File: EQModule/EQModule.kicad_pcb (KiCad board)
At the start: 2 copper layers, 30 x 38 mm, 13 parts, among them J1 SigIn, J2 SigOut, J3 TreblePot, J4 BassPot, J5 MidPot, J6 VolPot

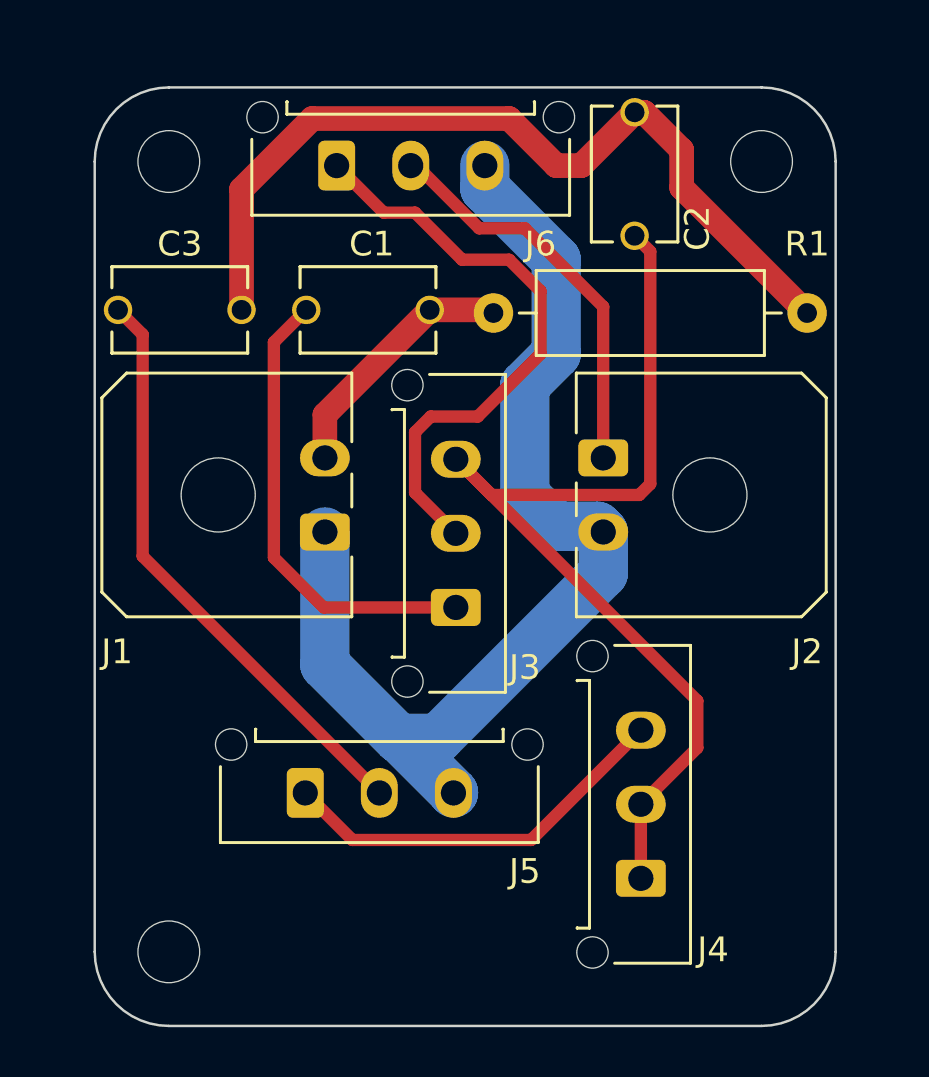
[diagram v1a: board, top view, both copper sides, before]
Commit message: Standardized hole size across all boards
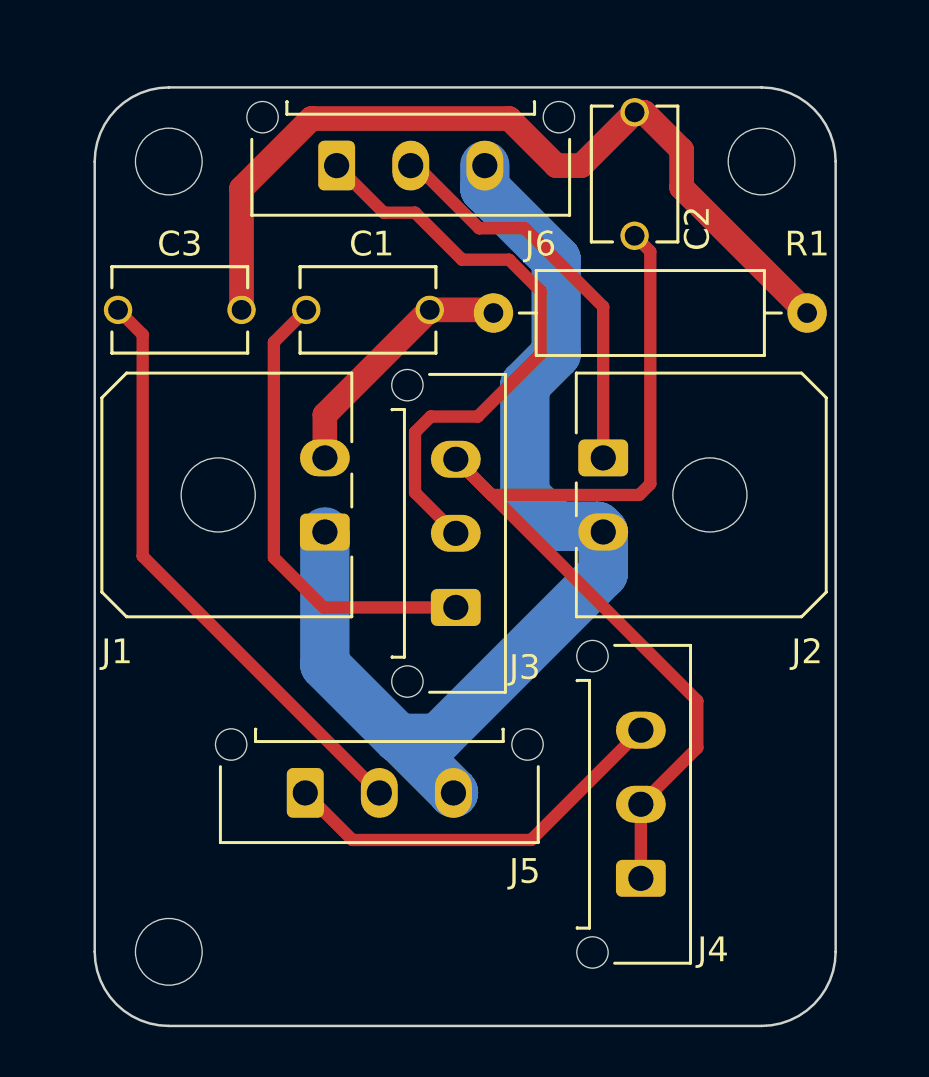
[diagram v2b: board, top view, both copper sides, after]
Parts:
- removed the REF** at (131.0, 50.0)
- removed the REF** at (155.0, 50.0)
- removed the REF** at (131.0, 82.0)
- added REF**: MountingHole_2.7mm_M2.5, MountingHole:MountingHole_2.7mm_M2.5, F.Cu at (131.0, 50.0)
- added REF**: MountingHole_2.7mm_M2.5, MountingHole:MountingHole_2.7mm_M2.5, F.Cu at (155.0, 50.0)
- added REF**: MountingHole_2.7mm_M2.5, MountingHole:MountingHole_2.7mm_M2.5, F.Cu at (131.0, 82.0)
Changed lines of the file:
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@@
     )
+  )
+  (footprint "MountingHole:MountingHole_2.7mm_M2.5" (layer "F.Cu")
+    (at 131 50)
+    (descr "Mounting Hole 2.7mm, no annular, M2.5")
+    (tags "mounting hole 2.7mm no annular m2.5")
+    (attr exclude_from_pos_files exclude_from_bom)
+    (fp_text reference "REF**" (at 0 -3.7) (layer "F.SilkS") hide
+        (effects (font (size 1 1) (thickness 0.15)))
+    )
+    (fp_text value "MountingHole_2.7mm_M2.5" (at 0 3.7) (layer "F.Fab") hide
+        (effects (font (size 1 1) (thickness 0.15)))
+    )
+    (fp_text user "${REFERENCE}" (at 0 0) (layer "F.Fab")
+        (effects (font (size 1 1) (thickness 0.15)))
+    )
+    (fp_circle (center 0 0) (end 2.7 0)
+      (stroke (width 0.15) (type solid)) (fill none) (layer "Cmts.User"))
+    (fp_circle (center 0 0) (end 2.95 0)
+      (stroke (width 0.05) (type solid)) (fill none) (layer "F.CrtYd"))
+    (pad "" np_thru_hole circle (at 0 0) (size 2.7 2.7) (drill 2.7) (layers "*.Cu" "*.Mask"))
   )
   (footprint "Resistor_THT:R_Axial_DIN0309_L9.0mm_D3.2mm_P12.70mm_Horizontal" (layer "F.Cu")
@@
       (rotate (xyz 0 0 0))
     )
+  )
+  (footprint "MountingHole:MountingHole_2.7mm_M2.5" (layer "F.Cu")
+    (at 155 50)
+    (descr "Mounting Hole 2.7mm, no annular, M2.5")
+    (tags "mounting hole 2.7mm no annular m2.5")
+    (attr exclude_from_pos_files exclude_from_bom)
+    (fp_text reference "REF**" (at 0 -3.7) (layer "F.SilkS") hide
+        (effects (font (size 1 1) (thickness 0.15)))
+    )
+    (fp_text value "MountingHole_2.7mm_M2.5" (at 0 3.7) (layer "F.Fab") hide
+        (effects (font (size 1 1) (thickness 0.15)))
+    )
+    (fp_text user "${REFERENCE}" (at 0 0) (layer "F.Fab")
+        (effects (font (size 1 1) (thickness 0.15)))
+    )
+    (fp_circle (center 0 0) (end 2.7 0)
+      (stroke (width 0.15) (type solid)) (fill none) (layer "Cmts.User"))
+    (fp_circle (center 0 0) (end 2.95 0)
+      (stroke (width 0.05) (type solid)) (fill none) (layer "F.CrtYd"))
+    (pad "" np_thru_hole circle (at 0 0) (size 2.7 2.7) (drill 2.7) (layers "*.Cu" "*.Mask"))
   )
   (footprint "CustomFootprints:Molex_Micro-Fit_3.0_43650-0315_1x03_P3.00mm_Vertical" (layer "F.Cu")
@@
     )
   )
-  (footprint "MountingHole:MountingHole_2.5mm" (layer "F.Cu")
-    (at 131 50)
-    (descr "Mounting Hole 2.5mm, no annular")
-    (tags "mounting hole 2.5mm no annular")
-    (attr exclude_from_pos_files exclude_from_bom)
-    (fp_text reference "REF**" (at 0 -3.5) (layer "F.SilkS") hide
-        (effects (font (size 1 1) (thickness 0.15)))
-    )
-    (fp_text value "MountingHole_2.5mm" (at 0 3.5) (layer "F.Fab") hide
-        (effects (font (size 1 1) (thickness 0.15)))
-    )
-    (fp_text user "${REFERENCE}" (at 0 0) (layer "F.Fab")
-        (effects (font (size 1 1) (thickness 0.15)))
-    )
-    (fp_circle (center 0 0) (end 2.5 0)
-      (stroke (width 0.15) (type solid)) (fill none) (layer "Cmts.User"))
-    (fp_circle (center 0 0) (end 2.75 0)
-      (stroke (width 0.05) (type solid)) (fill none) (layer "F.CrtYd"))
-    (pad "" np_thru_hole circle (at 0 0) (size 2.5 2.5) (drill 2.5) (layers "F&B.Cu" "*.Mask"))
-  )
   (footprint "CustomFootprints:Molex_Micro-Fit_3.0_43650-0315_1x03_P3.00mm_Vertical" (layer "F.Cu")
     (at 142.621 68.055 90)
@@
     )
   )
+  (footprint "MountingHole:MountingHole_2.7mm_M2.5" (layer "F.Cu")
+    (at 131 82)
+    (descr "Mounting Hole 2.7mm, no annular, M2.5")
+    (tags "mounting hole 2.7mm no annular m2.5")
+    (attr exclude_from_pos_files exclude_from_bom)
+    (fp_text reference "REF**" (at 0 -3.7) (layer "F.SilkS") hide
+        (effects (font (size 1 1) (thickness 0.15)))
+    )
+    (fp_text value "MountingHole_2.7mm_M2.5" (at 0 3.7) (layer "F.Fab") hide
+        (effects (font (size 1 1) (thickness 0.15)))
+    )
+    (fp_text user "${REFERENCE}" (at 0 0) (layer "F.Fab")
+        (effects (font (size 1 1) (thickness 0.15)))
+    )
+    (fp_circle (center 0 0) (end 2.7 0)
+      (stroke (width 0.15) (type solid)) (fill none) (layer "Cmts.User"))
+    (fp_circle (center 0 0) (end 2.95 0)
+      (stroke (width 0.05) (type solid)) (fill none) (layer "F.CrtYd"))
+    (pad "" np_thru_hole circle (at 0 0) (size 2.7 2.7) (drill 2.7) (layers "*.Cu" "*.Mask"))
+  )
   (footprint "CustomFootprints:FG26 Cap" (layer "F.Cu")
     (at 149.86 50.506 -90)
@@
       (rotate (xyz -90 0 0))
     )
-  )
-  (footprint "MountingHole:MountingHole_2.5mm" (layer "F.Cu")
-    (at 155 50)
-    (descr "Mounting Hole 2.5mm, no annular")
-    (tags "mounting hole 2.5mm no annular")
-    (attr exclude_from_pos_files exclude_from_bom)
-    (fp_text reference "REF**" (at 0 -3.5) (layer "F.SilkS") hide
-        (effects (font (size 1 1) (thickness 0.15)))
-    )
-    (fp_text value "MountingHole_2.5mm" (at 0 3.5) (layer "F.Fab") hide
-        (effects (font (size 1 1) (thickness 0.15)))
-    )
-    (fp_text user "${REFERENCE}" (at 0 0) (layer "F.Fab")
-        (effects (font (size 1 1) (thickness 0.15)))
-    )
-    (fp_circle (center 0 0) (end 2.5 0)
-      (stroke (width 0.15) (type solid)) (fill none) (layer "Cmts.User"))
-    (fp_circle (center 0 0) (end 2.75 0)
-      (stroke (width 0.05) (type solid)) (fill none) (layer "F.CrtYd"))
-    (pad "" np_thru_hole circle (at 0 0) (size 2.5 2.5) (drill 2.5) (layers "F&B.Cu" "*.Mask"))
-  )
-  (footprint "MountingHole:MountingHole_2.5mm" (layer "F.Cu")
-    (at 131 82)
-    (descr "Mounting Hole 2.5mm, no annular")
-    (tags "mounting hole 2.5mm no annular")
-    (attr exclude_from_pos_files exclude_from_bom)
-    (fp_text reference "REF**" (at 0 -3.5) (layer "F.SilkS") hide
-        (effects (font (size 1 1) (thickness 0.15)))
-    )
-    (fp_text value "MountingHole_2.5mm" (at 0 3.5) (layer "F.Fab") hide
-        (effects (font (size 1 1) (thickness 0.15)))
-    )
-    (fp_text user "${REFERENCE}" (at 0 0) (layer "F.Fab")
-        (effects (font (size 1 1) (thickness 0.15)))
-    )
-    (fp_circle (center 0 0) (end 2.5 0)
-      (stroke (width 0.15) (type solid)) (fill none) (layer "Cmts.User"))
-    (fp_circle (center 0 0) (end 2.75 0)
-      (stroke (width 0.05) (type solid)) (fill none) (layer "F.CrtYd"))
-    (pad "" np_thru_hole circle (at 0 0) (size 2.5 2.5) (drill 2.5) (layers "F&B.Cu" "*.Mask"))
   )
   (gr_line (start 128 82) (end 128 50)
@@
   (segment (start 135.255 57.317) (end 135.255 66.04) (width 0.5) (layer "F.Cu") (net 2))
   (segment (start 136.565 56.007) (end 135.255 57.317) (width 0.5) (layer "F.Cu") (net 2))
-  (segment (start 144.78 48.26) (end 136.807285 48.26) (width 1) (layer "F.Cu") (net 3))
   (segment (start 156.845 56.134) (end 151.765 51.054) (width 1) (layer "F.Cu") (net 3))
   (segment (start 150.241 48.006) (end 149.86 48.006) (width 1) (layer "F.Cu") (net 3))
-  (segment (start 133.945 51.122285) (end 133.945 56.007) (width 1) (layer "F.Cu") (net 3))
+  (segment (start 147.701 50.165) (end 146.685 50.165) (width 1) (layer "F.Cu") (net 3))
+  (segment (start 136.773643 48.26) (end 133.945 51.088643) (width 1) (layer "F.Cu") (net 3))
+  (segment (start 146.685 50.165) (end 144.78 48.26) (width 1) (layer "F.Cu") (net 3))
   (segment (start 149.86 48.006) (end 147.701 50.165) (width 1) (layer "F.Cu") (net 3))
-  (segment (start 136.807285 48.26) (end 133.945 51.122285) (width 1) (layer "F.Cu") (net 3))
-  (segment (start 147.701 50.165) (end 146.685 50.165) (width 1) (layer "F.Cu") (net 3))
-  (segment (start 146.685 50.165) (end 144.78 48.26) (width 1) (layer "F.Cu") (net 3))
+  (segment (start 133.945 51.088643) (end 133.945 56.007) (width 1) (layer "F.Cu") (net 3))
+  (segment (start 144.78 48.26) (end 136.773643 48.26) (width 1) (layer "F.Cu") (net 3))
   (segment (start 151.765 51.054) (end 151.765 49.53) (width 1) (layer "F.Cu") (net 3))
   (segment (start 151.765 49.53) (end 150.241 48.006) (width 1) (layer "F.Cu") (net 3))
